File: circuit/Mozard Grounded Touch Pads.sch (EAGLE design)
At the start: 28 parts, among them J2 SPKR, J4 Headphone/Line Out, U2 LM386

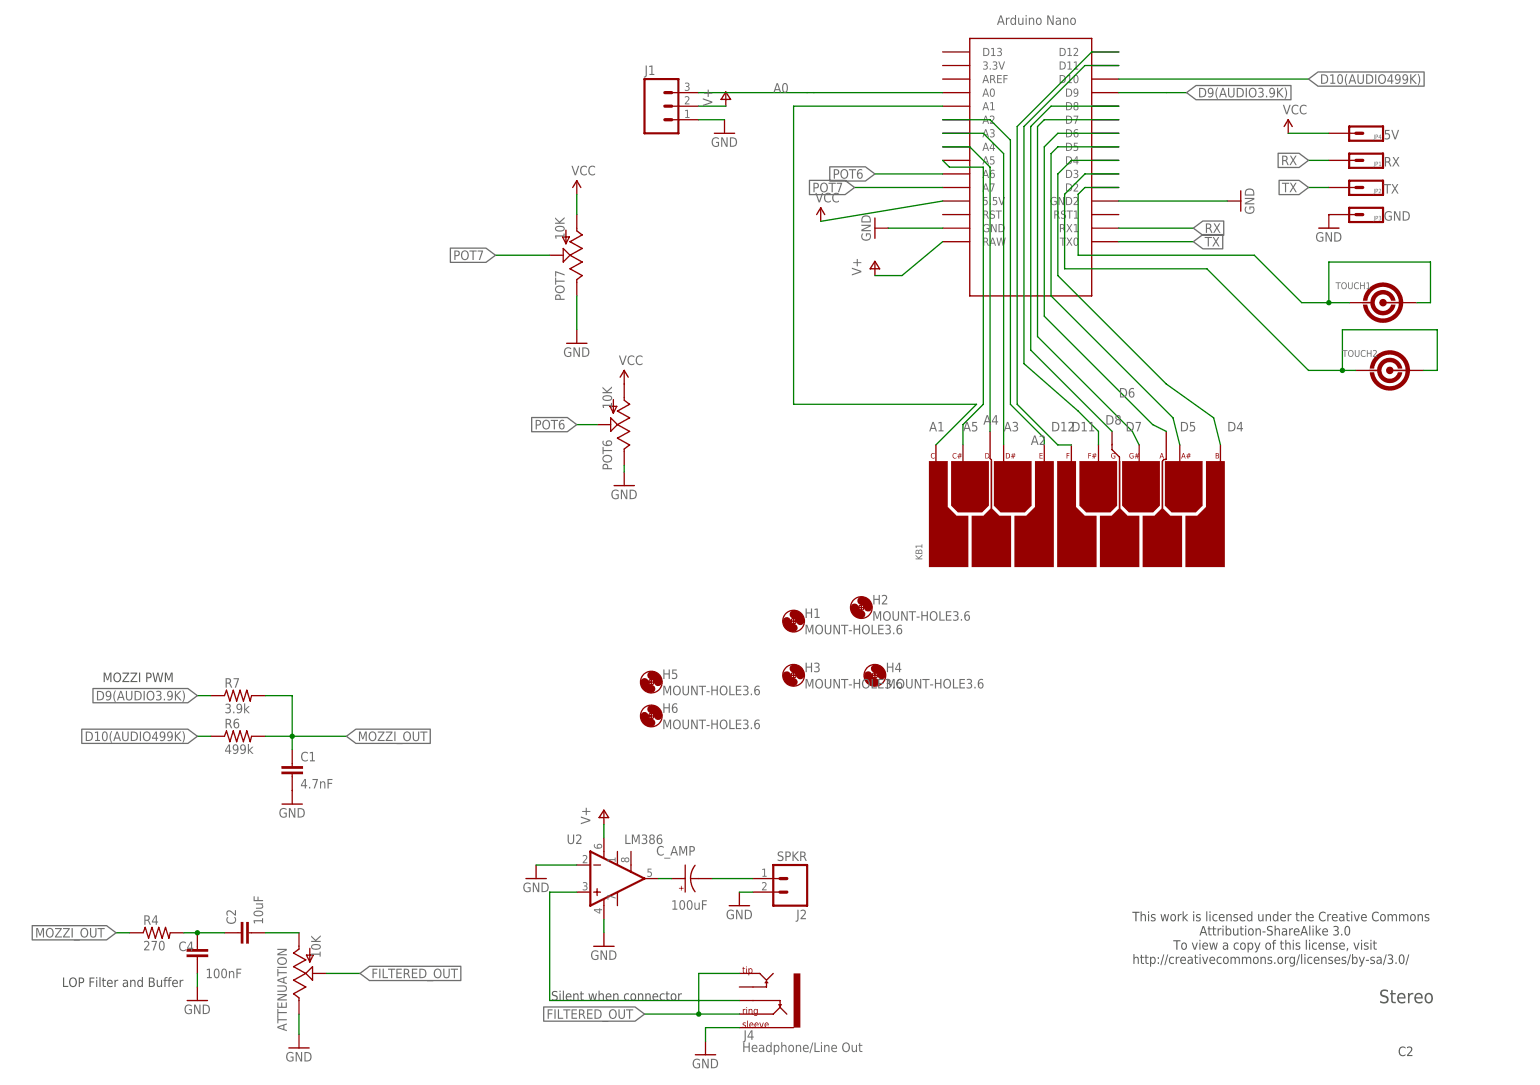
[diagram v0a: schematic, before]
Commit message: New version with grounded touch pads
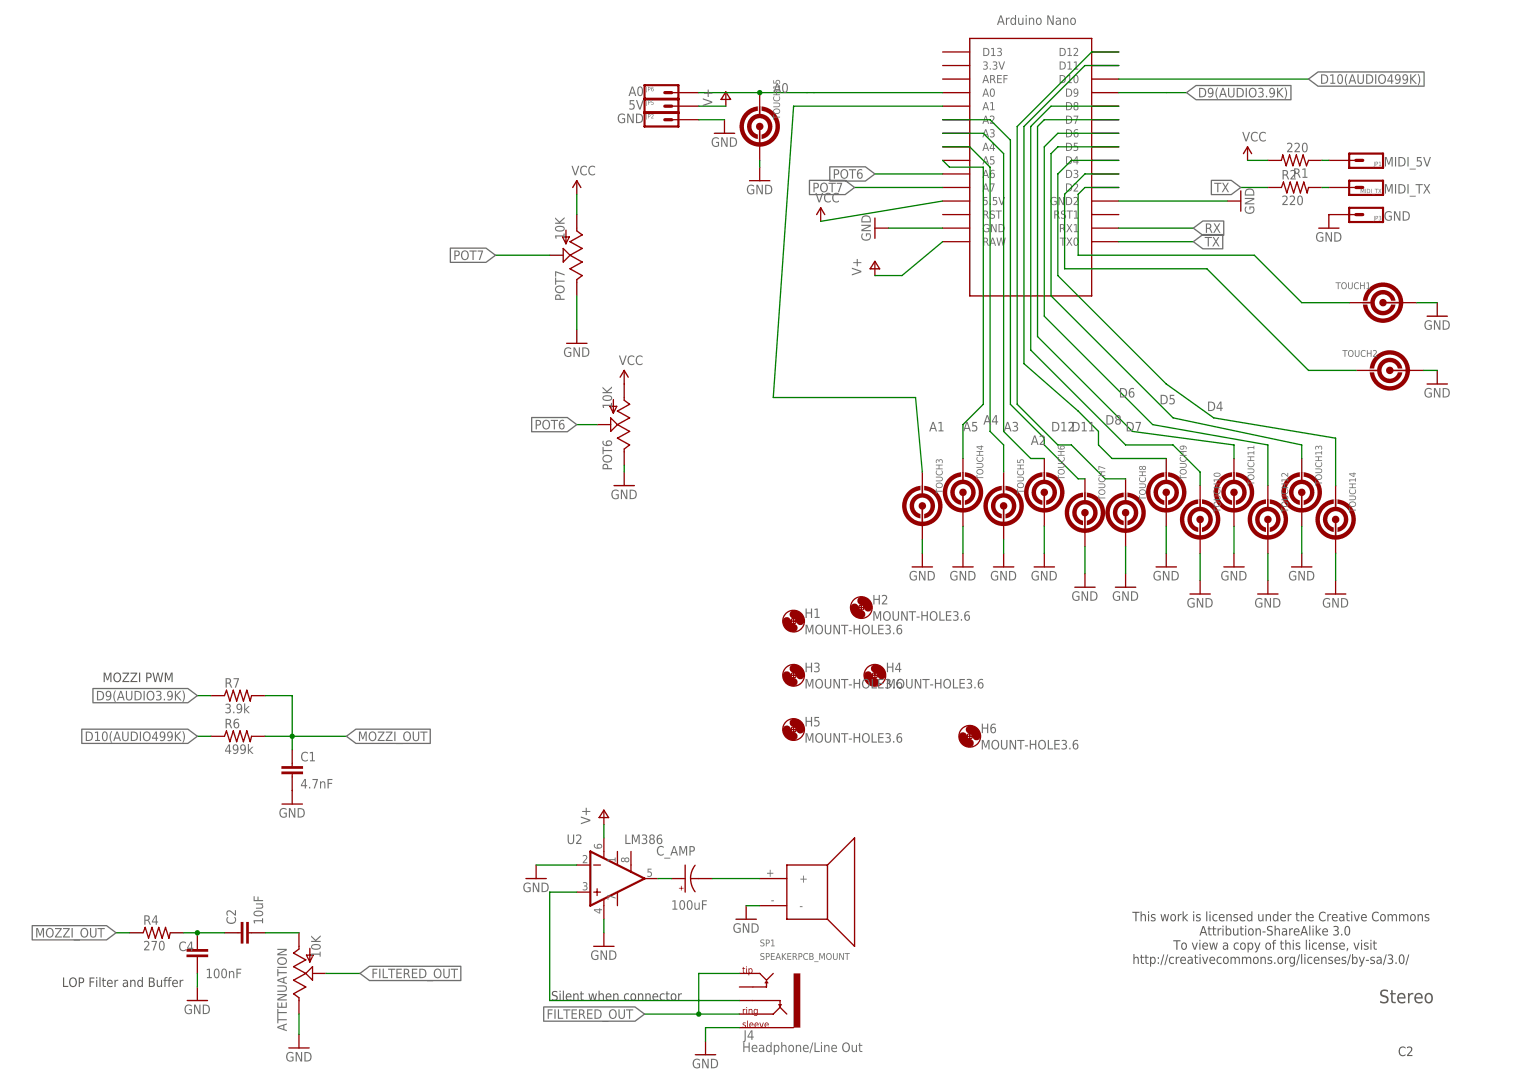
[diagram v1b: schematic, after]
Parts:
- removed J1: (no value), SparkFun-Connectors:M03SCREW
- removed J2: SPKR, SparkFun-Connectors:M023.5MM
- removed JP4: 5V, TOF:HEADER-1X1
- removed KB1: (no value), Mitch-parts:PCB-KEYBOARD4
- added JP5: 5V, TOF:HEADER-1X1
- added JP6: A0, TOF:HEADER-1X1
- added MIDI_TX: MIDI_TX, TOF:HEADER-1X1
- added R1, R2: 220, adafruit:R-US_0204/7
- added SP1: SPEAKERPCB_MOUNT, SparkFun-Electromechanical:SPEAKERPCB_MOUNT
- added TOUCH10, TOUCH11, TOUCH12, TOUCH13, TOUCH14, TOUCH15, TOUCH3, TOUCH4, TOUCH5, TOUCH6, TOUCH7, TOUCH8, TOUCH9: (no value), TOF:PCB-TOUCHPAD2
- JP1: value RX -> MIDI_5V
- JP2: value TX -> GND
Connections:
- new net N$3: JP1.1, R1.1
- new net N$5: MIDI_TX.1, R2.2
- net A0: now also JP6.1, TOUCH15.1; no longer J1.3
- net A1: now also TOUCH3.1; no longer KB1.C
- net A2: now also TOUCH7.1; no longer KB1.E
- net A3: now also TOUCH6.1; no longer KB1.D#
- net A4: now also TOUCH5.1; no longer KB1.D
- net A5: now also TOUCH4.1; no longer KB1.C#
- net D11: now also TOUCH9.1; no longer KB1.F#
- net D12: now also TOUCH8.1; no longer KB1.F
- net D4: now also TOUCH14.1; no longer KB1.B
- net D5: now also TOUCH13.1; no longer KB1.A#
- net D6: now also TOUCH12.1; no longer KB1.A
- net D7: now also TOUCH11.1; no longer KB1.G#
- net D8: now also TOUCH10.1; no longer KB1.G
- net GND: now also JP2.1, SP1.-, TOUCH1.2, TOUCH10.2, TOUCH11.2, TOUCH12.2, TOUCH13.2, TOUCH14.2, TOUCH15.2, TOUCH2.2, TOUCH3.2, TOUCH4.2, TOUCH5.2, TOUCH6.2, TOUCH7.2, TOUCH8.2, TOUCH9.2; no longer J1.1, J2.2
- net N$1: now also SP1.+; no longer J2.1
- net RX: no longer JP1.1
- net TOUCH_A: no longer TOUCH1.2
- net TOUCH_B: no longer TOUCH2.2
- net TX: now also R2.1; no longer JP2.1
- net V+: now also JP5.1; no longer J1.2
- net VCC: now also R1.2; no longer JP4.1
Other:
- moved on the sheet: H5, H6, JP2
